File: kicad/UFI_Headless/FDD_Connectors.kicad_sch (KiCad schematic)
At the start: 3 parts, among them J6 FDD_34PIN, J7 AMIGA_FDD

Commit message: UFI Headless: 4-layer layout v0.1, LCSC sourcing, fab outputs
- build_pcb.py: footprints from the schematic netlist (KIID-linked), placement,
  pre-routed USB-C fan-out and MCU VSS stubs, In1 GND plane
- make_pcb.sh: Freerouting 2.4.1 routing, violation cleanup, supply widening,
  GND/3V3 pours, stitching vias; DRC 0 errors, schematic parity clean
- LCSC part numbers via JLCPCB API; crystal X322525MOB4SI (CL 12pF, 2x 18pF)
- fertigung/: Gerber, Excellon, BOM/CPL (KiCad + JLC format)

Co-Authored-By: Claude Opus 5.5 <noreply@anthropic.com>
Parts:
- J6: LCSC (none) -> C20920
- RN6: LCSC (none) -> C20197

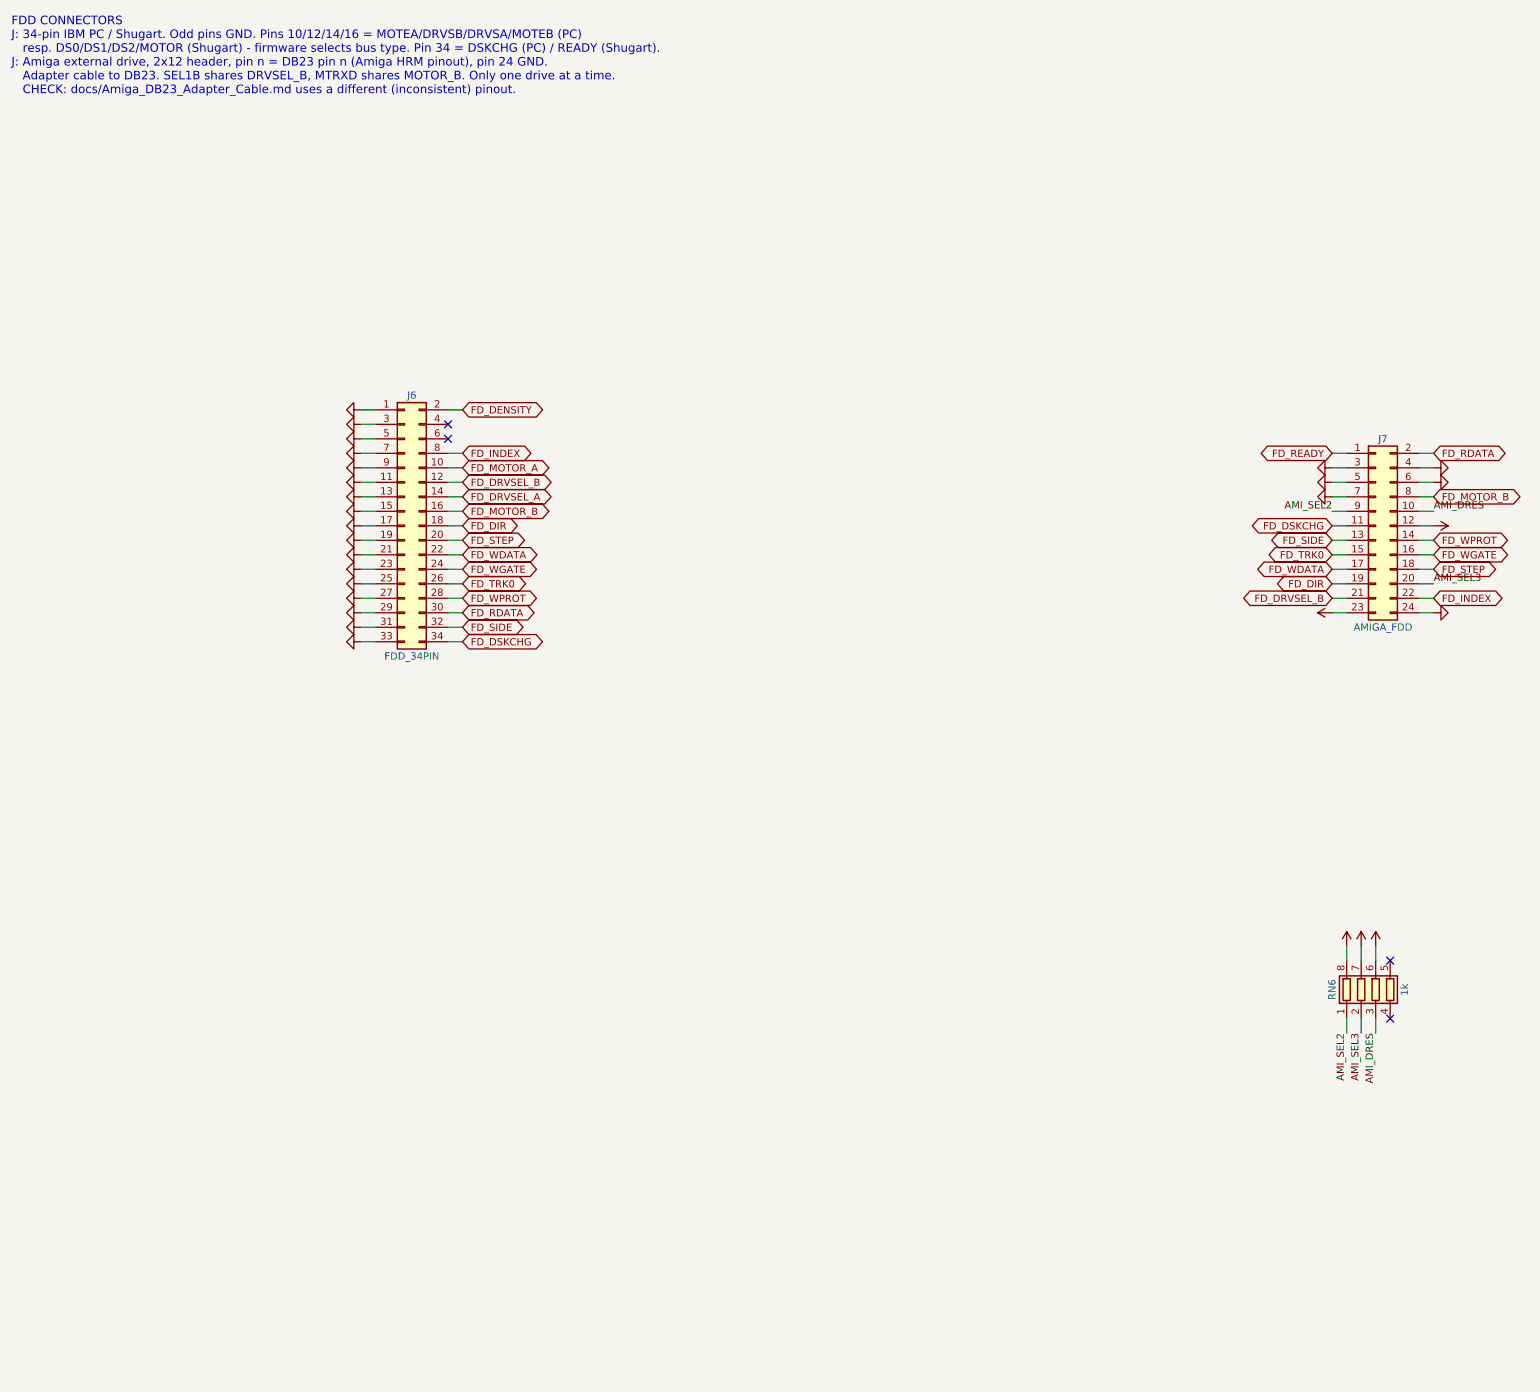
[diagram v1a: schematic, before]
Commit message: UFI Headless v0.2: 8 MB PSRAM, ESD, drive polyfuses, test points
Schematic (new parts get fixed references above the v0.1 maxima, so all
existing references and PCB links stay unchanged):
- U11 APS6404L 8 MB QSPI PSRAM on OCTOSPIM P1 (PB2/PB10/PD11/PD12/PB13/
  PD13), C46, CE# pull-up R16
- D9-D11 ESDA6V1-5SC6 on the 13 Amiga J7 bus lines + MOTOR_A, D12 on IEC
- F2/F3 polyfuses: drive supplies FDD_5V/FDD_12V for J3 and J7 pins 12/23
- TP1-TP6 (3V3, 5V, 12V, GND, RDATA, INDEX), excluded from BOM/CPL
Layout (incremental ECO on the reviewed board):
- scripts/add_parts.py: re-net pads, collision-aware placement, rip up only
  what is in the way; make_pcb.sh 'eco' step
- fixes found on the way: supply pours ran after finish_pcb and left GND
  islands (LDO U4 ground!) without vias -> order swapped, GND pour check
  per net; island/dogbone vias never inside pads; manual_routes no longer
  re-applies the D+ fallback; pipeline filters robust against interleaved
  SWIG noise under pipefail
- DRC rule for the intentional J6/J7 silk overhang instead of warnings;
  netclasses cover the new drive supply nets
DRC: 0 errors, 0 warnings, 0 unconnected, parity clean, no via-in-pad.

Co-Authored-By: Claude Opus 5.5 <noreply@anthropic.com>
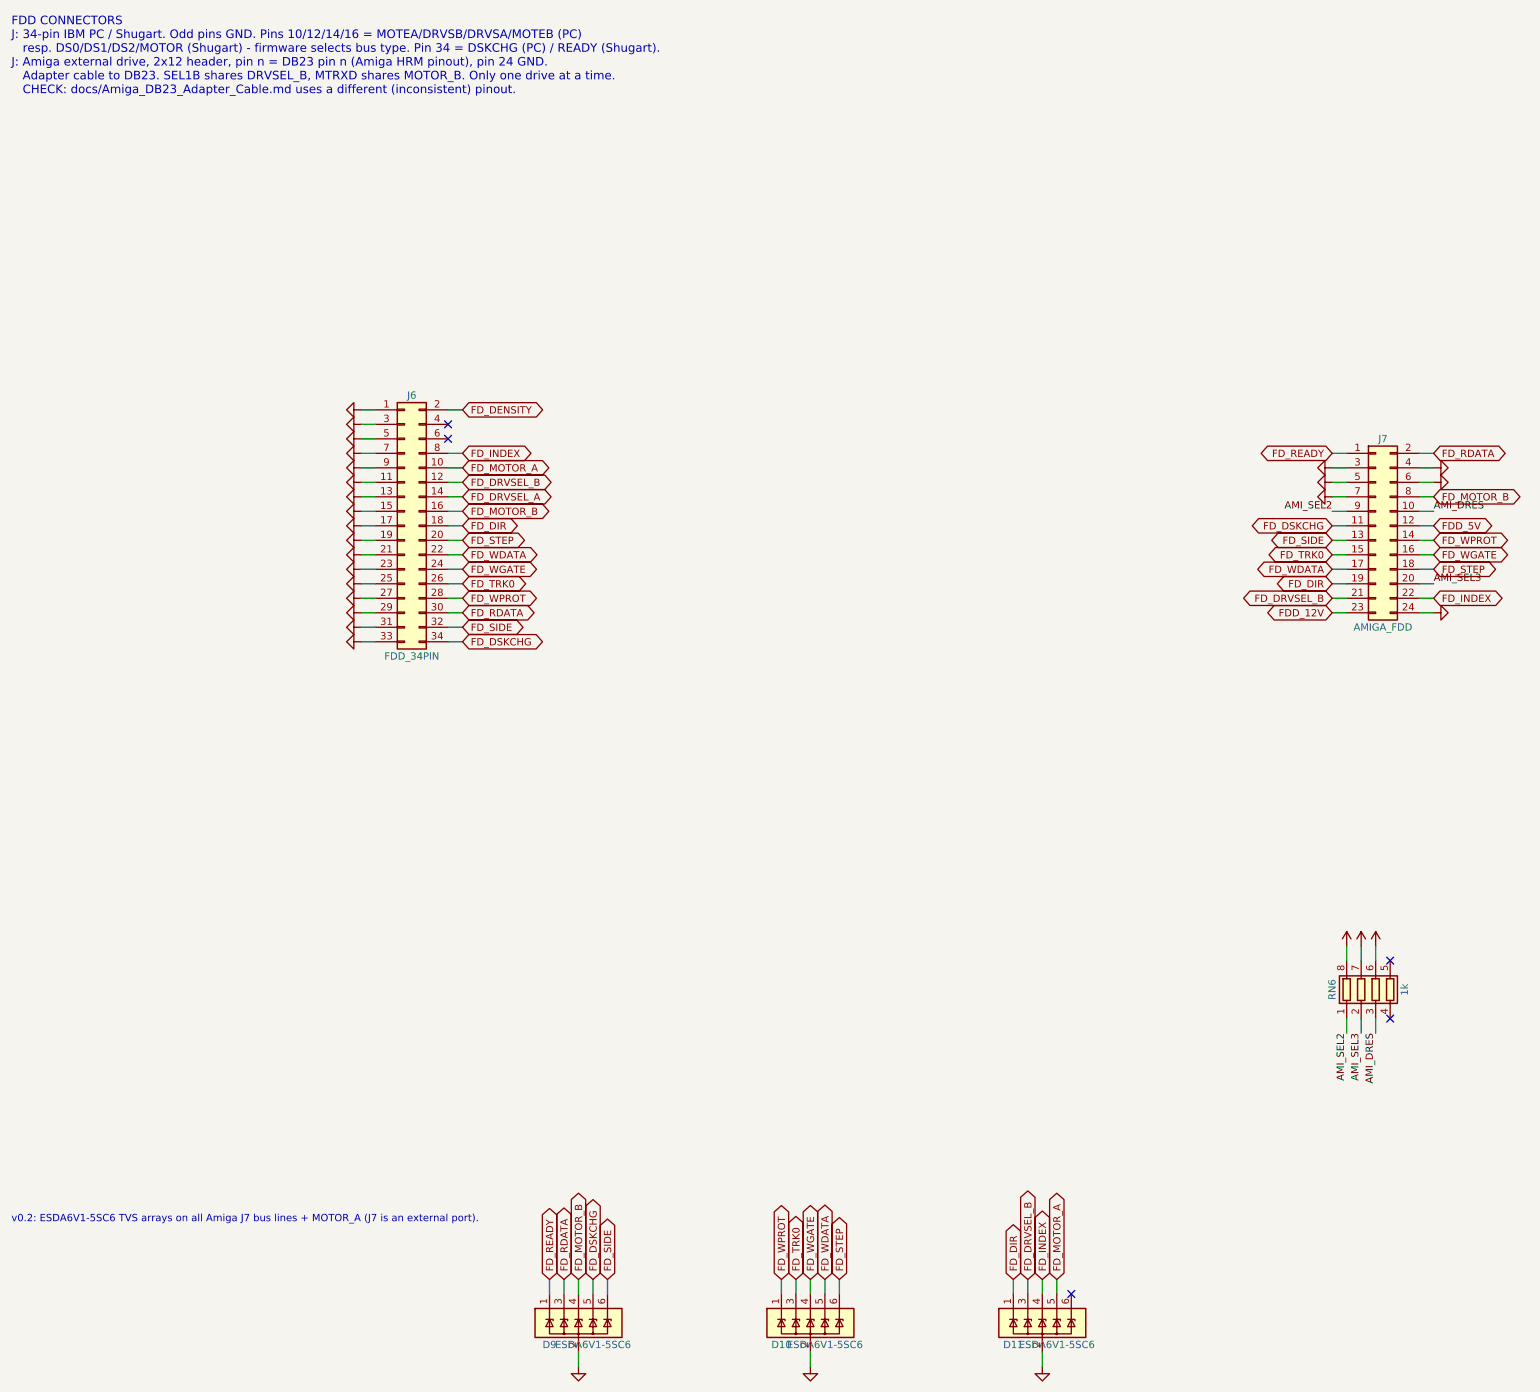
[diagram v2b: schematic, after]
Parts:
- added D10, D11, D9: ESDA6V1-5SC6, Package_TO_SOT_SMD:SOT-23-6, symbol Power_Protection:ESDA6V1-5SC6
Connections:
- net +5V: no longer J7.12 (Pin_12)
- net FD_DIR: now also D11.1 (IO1)
- net FD_DRVSEL_B: now also D11.3 (IO2)
- net FD_DSKCHG: now also D9.5 (IO4)
- net FD_INDEX: now also D11.4 (IO3)
- net FD_MOTOR_A: now also D11.5 (IO4)
- net FD_MOTOR_B: now also D9.4 (IO3)
- net FD_RDATA: now also D9.3 (IO2)
- net FD_READY: now also D9.1 (IO1)
- net FD_SIDE: now also D9.6 (IO5)
- net FD_STEP: now also D10.6 (IO5)
- net FD_TRK0: now also D10.3 (IO2)
- net FD_WDATA: now also D10.5 (IO4)
- net FD_WGATE: now also D10.4 (IO3)
- net FD_WPROT: now also D10.1 (IO1)
- net GND: now also D10.2 (GND), D11.2 (GND), D9.2 (GND)
- net +12V renamed FDD_12V
- new net FDD_5V: J7.12 (Pin_12)
- no-connect marks 4 -> 5
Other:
- note added: "v0.2: ESDA6V1-5SC6 TVS arrays on all Amiga J7 bus lines + MOTOR_A (J7 is an external port)."
